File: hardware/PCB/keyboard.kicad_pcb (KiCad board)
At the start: 2 copper layers, 282.7 x 111.3 mm, 251 parts, among them U1 proton_c, U2 IS31FL3733-QF, U3 IS31FL3733-QF

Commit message: Line up most parts and fix some problems with the part
1.Fix the LED footprint size
2.Edit the hotplug to be simpler (removed 2 holes)
3.Line up everything and the silkscreen
4. Fix the LED matrix and the switch matrix sch
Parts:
- removed D139, D140, D141, D96, D97: LED_RABG, KiCad:XZMDKCBDDG45S9
- added CherryMX67: SW_SPST, KiCad:Kailh_socket_MX_simplified, F.Cu at (347.4, 167.0)
- CherryMX1, CherryMX10, CherryMX11, CherryMX12, CherryMX13, CherryMX14, CherryMX15, CherryMX16, CherryMX17, CherryMX18, CherryMX19, CherryMX2, CherryMX20, CherryMX21, CherryMX22, CherryMX23, CherryMX24, CherryMX25, CherryMX26, CherryMX27, CherryMX28, CherryMX29, CherryMX3, CherryMX30, CherryMX31, CherryMX32, CherryMX33, CherryMX34, CherryMX35, CherryMX36, CherryMX37, CherryMX38, CherryMX39, CherryMX4, CherryMX40, CherryMX41, CherryMX42, CherryMX43, CherryMX44, CherryMX45, CherryMX46, CherryMX47, CherryMX48, CherryMX49, CherryMX5, CherryMX50, CherryMX51, CherryMX52, CherryMX53, CherryMX54, CherryMX55, CherryMX56, CherryMX57, CherryMX58, CherryMX59, CherryMX6, CherryMX60, CherryMX61, CherryMX62, CherryMX63, CherryMX64, CherryMX65, CherryMX66, CherryMX68, CherryMX7, CherryMX8, CherryMX9: footprint keyswitches:Kailh_socket_MX -> KiCad:Kailh_socket_MX_simplified
- D100, D101, D102, D103, D104, D105, D106, D107, D108, D109, D110, D111, D112, D113, D114, D115, D116, D117, D118, D119, D120, D121, D122, D123, D124, D125, D126, D127, D128, D129, D130, D131, D132, D133, D134, D135, D136, D137, D138, D69, D70, D71, D72, D73, D74, D75, D76, D77, D78, D79, D80, D81, D82, D83, D84, D85, D86, D87, D88, D89, D90, D91, D92, D93, D94, D95, D98, D99: footprint KiCad:XZMDKCBDDG45S9 -> KiCad:XZMDKCBDDG45S9_fixed
- moved D67 604.6 mm to (354.3, 165.1), turned to 180 degrees
- moved D94 601.5 mm to (347.4, 162.5)
- moved D60 590.2 mm to (337.8, 106.7), turned to 180 degrees
- moved D95 589.7 mm to (347.4, 181.5)
- moved D66 585.0 mm to (356.9, 124.5), turned to 180 degrees
- moved D92 574.6 mm to (328.3, 162.5)
- moved D68 572.2 mm to (354.3, 184.2), turned to 180 degrees
- moved CherryMX66 565.8 mm to (347.4, 128.9), turned to 180 degrees
- moved D90 564.8 mm to (309.3, 162.5)
- moved D64 563.3 mm to (337.8, 182.9), turned to 180 degrees
- moved U2 557.9 mm to (353.3, 142.0), turned to 90 degrees
- moved D46 538.7 mm to (280.7, 127.0), turned to 180 degrees
- moved D86 528.4 mm to (271.2, 162.5)
- moved D44 526.6 mm to (261.6, 180.3), turned to 180 degrees
- moved D59 526.0 mm to (318.8, 182.9), turned to 180 degrees
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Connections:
- U2 pad 32: /RGB/RGBmatrix/COL15 -> Net-(U2-Pad32)
- U3 pad 32: /RGB/RGBmatrix2/COL15 -> Net-(U3-Pad32)

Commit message: I think I figured it out
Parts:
- U1: value proton_c -> Proton_C
- moved C11 339.1 mm to (404.9, 170.9)
- moved C12 335.6 mm to (404.9, 174.8)
- moved C15 331.1 mm to (394.7, 170.9)
- moved C16 328.0 mm to (394.7, 174.8)
- moved R22 327.1 mm to (389.6, 178.6)
- moved U3 324.3 mm to (399.8, 182.4)
- moved C13 323.1 mm to (399.8, 170.9)
- moved R24 322.4 mm to (384.6, 183.6)
- moved C2 321.2 mm to (384.6, 178.6)
- moved R21 319.1 mm to (384.6, 181.1)
- moved R20 318.5 mm to (389.6, 181.1)
- moved C10 310.7 mm to (387.1, 172.2)
- moved R15 305.3 mm to (389.6, 183.6)
- moved C14 289.6 mm to (399.8, 174.8)
- moved R17 266.8 mm to (388.6, 130.8)
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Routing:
- net /switch/ROW1: track 0.00 -> 291.9 mm
- net /switch/ROW4: track 0.00 -> 291.9 mm
- net /switch/ROW2: track 0.00 -> 291.9 mm
- net /switch/ROW5: track 0.00 -> 288.6 mm
- net /switch/ROW3: track 0.00 -> 278.9 mm
- net /switch/COL2: track 0.00 -> 99.3 mm, vias 0 -> 5
- net /switch/COL1: track 0.00 -> 90.9 mm, vias 0 -> 4
- net /switch/COL9: track 0.00 -> 90.9 mm, vias 0 -> 5
- net /switch/COL4: track 0.00 -> 89.2 mm, vias 0 -> 5
- net /switch/COL7: track 0.00 -> 89.2 mm, vias 0 -> 5
- net /switch/COL10: track 0.00 -> 89.2 mm, vias 0 -> 5
- net /switch/COL14: track 0.00 -> 89.2 mm, vias 0 -> 5
- net /switch/COL13: track 0.00 -> 89.2 mm, vias 0 -> 5
- net /switch/COL3: track 0.00 -> 89.2 mm, vias 0 -> 5
- net /switch/COL6: track 0.00 -> 89.2 mm, vias 0 -> 5
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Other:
- rule trace_min: 0.2 -> 0.1
- rule via_min_size: 0.4 -> 0.3

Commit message: The keys are finally connected
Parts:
- moved R15 197.3 mm to (197.6, 229.1)
- moved R20 197.3 mm to (197.6, 226.6)
- moved R22 197.3 mm to (197.6, 224.0)
- moved C10 197.3 mm to (195.1, 217.7)
- moved C13 197.3 mm to (207.8, 216.4)
- moved C14 197.3 mm to (207.8, 220.2)
- moved C15 197.3 mm to (202.7, 216.4)
- moved C16 197.3 mm to (202.7, 220.2)
- moved U3 197.3 mm to (207.8, 227.8)
- moved C11 197.3 mm to (212.9, 216.4)
- moved C12 197.3 mm to (212.9, 220.2)
- moved C2 197.3 mm to (192.5, 224.0)
- moved R21 197.3 mm to (192.5, 226.6)
- moved R24 197.3 mm to (192.5, 229.1)
- moved D1 0.25 mm to (92.5, 110.7)
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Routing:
- net /RGB/RGBmatrix2/ROW3: track 0.00 -> 288.7 mm
- net /RGB/RGBmatrix/ROW6: track 0.00 -> 288.7 mm
- net /RGB/RGBmatrix2/ROW5: track 0.00 -> 279.4 mm, vias 0 -> 24
- net /RGB/RGBmatrix/ROW9: track 0.00 -> 275.9 mm
- net /RGB/RGBmatrix2/ROW2: track 0.00 -> 274.1 mm, vias 0 -> 26
- net /RGB/RGBmatrix/ROW5: track 0.00 -> 274.1 mm, vias 0 -> 26
- net /RGB/RGBmatrix2/ROW1: track 0.00 -> 272.7 mm
- net /RGB/RGBmatrix/ROW4: track 0.00 -> 272.7 mm
- net /RGB/RGBmatrix/ROW3: track 23.2 -> 289.6 mm
- net /RGB/RGBmatrix/ROW8: track 0.00 -> 263.9 mm, vias 0 -> 23
- net /RGB/RGBmatrix/ROW7: track 0.00 -> 261.3 mm
- net /RGB/RGBmatrix/ROW2: track 21.1 -> 274.1 mm, vias 2 -> 26
- net /RGB/RGBmatrix/ROW1: track 20.9 -> 272.7 mm
- net /RGB/RGBmatrix2/ROW4: track 0.00 -> 241.8 mm
- net /RGB/RGBmatrix2/ROW6: track 0.00 -> 216.7 mm
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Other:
- net class Default: clearance 0.2 -> 0.15; trace_width 0.25 -> 0.3; via_dia 0.8 -> 1.2; via_drill 0.4 -> 0.5
- rule trace_clearance: 0.2 -> 0.15
- rule trace_min: 0.1 -> 0.3

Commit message: Make it better by get rid of the protonC
1. Remove protonC. use STM32F303CCT6 instead
2.Use parts based on avalibility
3.Extend the case so it now fits more parts( should be big enough
4. A reasonable USB connector
5. Probably a working DC-DC solution to providde 3.3V
6. Move 3733's 5V to only 3.3V (maybe it won't work?)
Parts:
- added C17: 1μF, Capacitor_SMD:C_0603_1608Metric, F.Cu at (239.6, 67.9)
- added C18: 100nF, Capacitor_SMD:C_0603_1608Metric, F.Cu at (241.2, 60.4)
- added C19: 10nF, Capacitor_SMD:C_0603_1608Metric, F.Cu at (231.6, 68.2)
- added C20: 1μF, Capacitor_SMD:C_0603_1608Metric, F.Cu at (248.7, 53.2)
- added C21: 20pF, Capacitor_SMD:C_0603_1608Metric, F.Cu at (241.2, 62.9)
- added C22: 20pF, Capacitor_SMD:C_0603_1608Metric, F.Cu at (235.6, 68.2)
- added C23: 1μF, Capacitor_SMD:C_0603_1608Metric, F.Cu at (245.2, 57.9)
- added D96: BAT60JFILM, Diode_SMD:D_SOD-323, F.Cu at (231.7, 65.4)
- added J1: USB_B_Micro, Connector_USB:USB_Micro-B_Molex-105017-0001, F.Cu at (236.9, 54.9)
- added R25: 1.5K, Resistor_SMD:R_0603_1608Metric, F.Cu at (245.2, 60.4)
- added R26: 0, Resistor_SMD:R_0603_1608Metric, F.Cu at (239.8, 65.4)
- added R27: 0, Resistor_SMD:R_0603_1608Metric, F.Cu at (235.8, 65.2)
- added R28: 100K, Resistor_SMD:R_0603_1608Metric, F.Cu at (249.2, 55.7)
- added R29: 1K, Resistor_SMD:R_0603_1608Metric, F.Cu at (249.2, 58.2)
- added R30: 10K, Resistor_SMD:R_0603_1608Metric, F.Cu at (245.2, 62.9)
- added R31: 10K, Resistor_SMD:R_0603_1608Metric, F.Cu at (249.2, 60.7)
- added R32: 0, Resistor_SMD:R_0603_1608Metric, F.Cu at (243.6, 67.9)
- added R33: 0, Resistor_SMD:R_0603_1608Metric, F.Cu at (249.2, 63.2)
- added SW1: SW_DIP_x01, Button_Switch_SMD:SW_SPST_EVQPE1, F.Cu at (225.1, 65.8)
- added U4: LD3985M33R, Package_TO_SOT_SMD:SOT-23-5, F.Cu at (244.2, 54.3)
- added Y1: YSX530GA, Crystal:Crystal_SMD_5032-2Pin_5.0x3.2mm, F.Cu at (235.6, 61.5)
- C1, C11, C13, C15, C2, C4, C6, C8: footprint Capacitor_SMD:C_0603_1608Metric_Pad1.05x0.95mm_HandSolder -> Capacitor_SMD:C_1206_3216Metric
- C10, C3: footprint Capacitor_Tantalum_SMD:CP_EIA-3528-12_Kemet-T_Pad1.50x2.35mm_HandSolder -> Capacitor_Tantalum_SMD:CP_EIA-3216-18_Kemet-A
- C12, C14, C16, C5, C7, C9: footprint Capacitor_SMD:C_0603_1608Metric_Pad1.05x0.95mm_HandSolder -> Capacitor_SMD:C_0603_1608Metric
- D1, D10, D11, D12, D13, D14, D15, D16, D17, D18, D19, D2, D20, D21, D22, D23, D24, D25, D26, D27, D28, D29, D3, D30, D31, D32, D33, D34, D35, D36, D37, D38, D39, D4, D40, D41, D42, D43, D44, D45, D46, D47, D48, D49, D5, D50, D51, D52, D53, D54, D55, D56, D57, D58, D59, D6, D60, D61, D62, D63, D64, D65, D66, D67, D68, D7, D8, D9: footprint Diode_SMD:D_SOD-123 -> Diode_SMD:D_SOD-323
- R1, R10, R11, R12, R13, R14, R15, R16, R17, R18, R19, R2, R20, R21, R22, R23, R24, R3, R4, R5, R6, R7, R8, R9: footprint Resistor_SMD:R_0603_1608Metric_Pad1.05x0.95mm_HandSolder -> Resistor_SMD:R_0603_1608Metric
- U1: value Proton_C -> STM32F303CCTx; footprint proton_c:proton_c -> Package_QFP:LQFP-48_7x7mm_P0.5mm; moved to F.Cu
- moved U3 156.4 mm to (184.8, 73.2)
- moved R15 150.6 mm to (211.5, 79.1)
- moved R20 150.6 mm to (211.5, 76.6)
- moved R21 150.6 mm to (206.4, 76.6)
- moved R24 150.6 mm to (206.4, 79.1)
- moved C2 150.6 mm to (206.4, 74.0)
- moved R22 150.6 mm to (211.5, 74.0)
- moved C12 139.8 mm to (193.5, 81.8), turned to 180 degrees
- moved C11 137.5 mm to (193.5, 80.3), turned to 180 degrees
- moved C13 136.9 mm to (186.7, 81.2)
- moved C14 136.9 mm to (186.7, 85.0)
- moved C15 136.9 mm to (181.6, 81.2)
- moved C16 136.9 mm to (181.6, 85.0)
- moved C10 135.0 mm to (199.6, 82.8)
- moved U2 108.5 mm to (294.3, 94.4)
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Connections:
- C1 pad 2: VCC -> +3V3
- C10 pad 1: VBUS -> +3V3
- C11 pad 1: VBUS -> +3V3
- C12 pad 1: VBUS -> +3V3
- C13 pad 1: VBUS -> +3V3
- C14 pad 1: VBUS -> +3V3
- C15 pad 1: VBUS -> +3V3
- C16 pad 1: VBUS -> +3V3
- C2 pad 2: VCC -> +3V3
- C3 pad 1: VBUS -> +3V3
- C4 pad 1: VBUS -> +3V3
- C5 pad 1: VBUS -> +3V3
- C6 pad 1: VBUS -> +3V3
- C7 pad 1: VBUS -> +3V3
- C8 pad 1: VBUS -> +3V3
- C9 pad 1: VBUS -> +3V3
- CherryMX1 pad 1: /switch/ROW1 -> /SMT32/ROW1
- CherryMX10 pad 1: /switch/ROW5 -> /SMT32/ROW5
- CherryMX11 pad 1: /switch/ROW1 -> /SMT32/ROW1
- CherryMX12 pad 1: /switch/ROW2 -> /SMT32/ROW2
- CherryMX13 pad 1: /switch/ROW3 -> /SMT32/ROW3
- CherryMX14 pad 1: /switch/ROW4 -> /SMT32/ROW4
- CherryMX15 pad 1: /switch/ROW5 -> /SMT32/ROW5
- CherryMX16 pad 1: /switch/ROW1 -> /SMT32/ROW1
- CherryMX17 pad 1: /switch/ROW2 -> /SMT32/ROW2
- CherryMX18 pad 1: /switch/ROW3 -> /SMT32/ROW3
- CherryMX19 pad 1: /switch/ROW4 -> /SMT32/ROW4
- CherryMX2 pad 1: /switch/ROW2 -> /SMT32/ROW2
- CherryMX20 pad 1: /switch/ROW5 -> /SMT32/ROW5
- CherryMX21 pad 1: /switch/ROW1 -> /SMT32/ROW1
- CherryMX22 pad 1: /switch/ROW2 -> /SMT32/ROW2
- CherryMX23 pad 1: /switch/ROW3 -> /SMT32/ROW3
- CherryMX24 pad 1: /switch/ROW4 -> /SMT32/ROW4
- CherryMX25 pad 1: /switch/ROW5 -> /SMT32/ROW5
- CherryMX26 pad 1: /switch/ROW1 -> /SMT32/ROW1
- CherryMX27 pad 1: /switch/ROW2 -> /SMT32/ROW2
- CherryMX28 pad 1: /switch/ROW3 -> /SMT32/ROW3
- CherryMX29 pad 1: /switch/ROW4 -> /SMT32/ROW4
- CherryMX3 pad 1: /switch/ROW3 -> /SMT32/ROW3
- CherryMX30 pad 1: /switch/ROW5 -> /SMT32/ROW5
- CherryMX31 pad 1: /switch/ROW1 -> /SMT32/ROW1
- CherryMX32 pad 1: /switch/ROW2 -> /SMT32/ROW2
- CherryMX33 pad 1: /switch/ROW3 -> /SMT32/ROW3
- CherryMX34 pad 1: /switch/ROW4 -> /SMT32/ROW4
- CherryMX35 pad 1: /switch/ROW1 -> /SMT32/ROW1
- CherryMX36 pad 1: /switch/ROW2 -> /SMT32/ROW2
- CherryMX37 pad 1: /switch/ROW3 -> /SMT32/ROW3
- CherryMX38 pad 1: /switch/ROW4 -> /SMT32/ROW4
- CherryMX39 pad 1: /switch/ROW5 -> /SMT32/ROW5
- CherryMX4 pad 1: /switch/ROW4 -> /SMT32/ROW4
- CherryMX40 pad 1: /switch/ROW1 -> /SMT32/ROW1
- CherryMX41 pad 1: /switch/ROW2 -> /SMT32/ROW2
- CherryMX42 pad 1: /switch/ROW3 -> /SMT32/ROW3
- CherryMX43 pad 1: /switch/ROW4 -> /SMT32/ROW4
- CherryMX44 pad 1: /switch/ROW5 -> /SMT32/ROW5
- CherryMX45 pad 1: /switch/ROW1 -> /SMT32/ROW1
- CherryMX46 pad 1: /switch/ROW2 -> /SMT32/ROW2
- CherryMX47 pad 1: /switch/ROW3 -> /SMT32/ROW3
- CherryMX48 pad 1: /switch/ROW4 -> /SMT32/ROW4
- CherryMX49 pad 1: /switch/ROW5 -> /SMT32/ROW5
- CherryMX5 pad 1: /switch/ROW5 -> /SMT32/ROW5
- CherryMX50 pad 1: /switch/ROW1 -> /SMT32/ROW1
- CherryMX51 pad 1: /switch/ROW2 -> /SMT32/ROW2
- CherryMX52 pad 1: /switch/ROW3 -> /SMT32/ROW3
- CherryMX53 pad 1: /switch/ROW4 -> /SMT32/ROW4
- CherryMX54 pad 1: /switch/ROW5 -> /SMT32/ROW5
- CherryMX55 pad 1: /switch/ROW1 -> /SMT32/ROW1
- CherryMX56 pad 1: /switch/ROW2 -> /SMT32/ROW2
- CherryMX57 pad 1: /switch/ROW3 -> /SMT32/ROW3
- CherryMX58 pad 1: /switch/ROW4 -> /SMT32/ROW4
- CherryMX59 pad 1: /switch/ROW5 -> /SMT32/ROW5
- CherryMX6 pad 1: /switch/ROW1 -> /SMT32/ROW1
- CherryMX60 pad 1: /switch/ROW1 -> /SMT32/ROW1
- CherryMX61 pad 1: /switch/ROW2 -> /SMT32/ROW2
- CherryMX62 pad 1: /switch/ROW3 -> /SMT32/ROW3
- CherryMX63 pad 1: /switch/ROW4 -> /SMT32/ROW4
- CherryMX64 pad 1: /switch/ROW5 -> /SMT32/ROW5
- CherryMX65 pad 1: /switch/ROW1 -> /SMT32/ROW1
- CherryMX66 pad 1: /switch/ROW2 -> /SMT32/ROW2
- CherryMX67 pad 1: /switch/ROW4 -> /SMT32/ROW4
- CherryMX68 pad 1: /switch/ROW5 -> /SMT32/ROW5
- CherryMX7 pad 1: /switch/ROW2 -> /SMT32/ROW2
- CherryMX8 pad 1: /switch/ROW3 -> /SMT32/ROW3
- CherryMX9 pad 1: /switch/ROW4 -> /SMT32/ROW4
- D1 pad 1: /switch/COL14 -> /SMT32/COL14
- D10 pad 1: /switch/COL13 -> /SMT32/COL13
- D11 pad 1: /switch/COL12 -> /SMT32/COL12
- D12 pad 1: /switch/COL12 -> /SMT32/COL12
- D13 pad 1: /switch/COL12 -> /SMT32/COL12
- D14 pad 1: /switch/COL12 -> /SMT32/COL12
- D15 pad 1: /switch/COL12 -> /SMT32/COL12
- D16 pad 1: /switch/COL11 -> /SMT32/COL11
- D17 pad 1: /switch/COL11 -> /SMT32/COL11
- D18 pad 1: /switch/COL11 -> /SMT32/COL11
- D19 pad 1: /switch/COL11 -> /SMT32/COL11
- D2 pad 1: /switch/COL14 -> /SMT32/COL14
- D20 pad 1: /switch/COL11 -> /SMT32/COL11
- D21 pad 1: /switch/COL10 -> /SMT32/COL10
- D22 pad 1: /switch/COL10 -> /SMT32/COL10
- D23 pad 1: /switch/COL10 -> /SMT32/COL10
- D24 pad 1: /switch/COL10 -> /SMT32/COL10
- D25 pad 1: /switch/COL10 -> /SMT32/COL10
- D26 pad 1: /switch/COL9 -> /SMT32/COL9
- D27 pad 1: /switch/COL9 -> /SMT32/COL9
- D28 pad 1: /switch/COL9 -> /SMT32/COL9
- D29 pad 1: /switch/COL9 -> /SMT32/COL9
- D3 pad 1: /switch/COL14 -> /SMT32/COL14
- D30 pad 1: /switch/COL9 -> /SMT32/COL9
- D31 pad 1: /switch/COL8 -> /SMT32/COL8
- D32 pad 1: /switch/COL8 -> /SMT32/COL8
- D33 pad 1: /switch/COL8 -> /SMT32/COL8
- D34 pad 1: /switch/COL8 -> /SMT32/COL8
- D35 pad 1: /switch/COL7 -> /SMT32/COL7
- D36 pad 1: /switch/COL7 -> /SMT32/COL7
- D37 pad 1: /switch/COL7 -> /SMT32/COL7
- D38 pad 1: /switch/COL7 -> /SMT32/COL7
- D39 pad 1: /switch/COL7 -> /SMT32/COL7
- D4 pad 1: /switch/COL14 -> /SMT32/COL14
- D40 pad 1: /switch/COL6 -> /SMT32/COL6
- D41 pad 1: /switch/COL6 -> /SMT32/COL6
- D42 pad 1: /switch/COL6 -> /SMT32/COL6
- D43 pad 1: /switch/COL6 -> /SMT32/COL6
- D44 pad 1: /switch/COL6 -> /SMT32/COL6
- D45 pad 1: /switch/COL5 -> /SMT32/COL5
- D46 pad 1: /switch/COL5 -> /SMT32/COL5
- D47 pad 1: /switch/COL5 -> /SMT32/COL5
- D48 pad 1: /switch/COL5 -> /SMT32/COL5
- D49 pad 1: /switch/COL5 -> /SMT32/COL5
- D5 pad 1: /switch/COL14 -> /SMT32/COL14
- D50 pad 1: /switch/COL4 -> /SMT32/COL4
- D51 pad 1: /switch/COL4 -> /SMT32/COL4
- D52 pad 1: /switch/COL4 -> /SMT32/COL4
- D53 pad 1: /switch/COL4 -> /SMT32/COL4
- D54 pad 1: /switch/COL4 -> /SMT32/COL4
- D55 pad 1: /switch/COL3 -> /SMT32/COL3
- D56 pad 1: /switch/COL3 -> /SMT32/COL3
- D57 pad 1: /switch/COL3 -> /SMT32/COL3
- D58 pad 1: /switch/COL3 -> /SMT32/COL3
- D59 pad 1: /switch/COL3 -> /SMT32/COL3
- D6 pad 1: /switch/COL13 -> /SMT32/COL13
- D60 pad 1: /switch/COL2 -> /SMT32/COL2
- D61 pad 1: /switch/COL2 -> /SMT32/COL2
- D62 pad 1: /switch/COL2 -> /SMT32/COL2
- D63 pad 1: /switch/COL2 -> /SMT32/COL2
- D64 pad 1: /switch/COL2 -> /SMT32/COL2
- D65 pad 1: /switch/COL1 -> /SMT32/COL1
- D66 pad 1: /switch/COL1 -> /SMT32/COL1
- D67 pad 1: /switch/COL1 -> /SMT32/COL1
- D68 pad 1: /switch/COL1 -> /SMT32/COL1
- D7 pad 1: /switch/COL13 -> /SMT32/COL13
- D8 pad 1: /switch/COL13 -> /SMT32/COL13
- D9 pad 1: /switch/COL13 -> /SMT32/COL13
- R1 pad 1: /switch/COL1 -> /SMT32/COL1
- R1 pad 2: VCC -> +3V3
- R10 pad 1: /switch/COL10 -> /SMT32/COL10
- R10 pad 2: VCC -> +3V3
- R11 pad 1: /switch/COL11 -> /SMT32/COL11
- R11 pad 2: VCC -> +3V3
- R12 pad 1: /switch/COL12 -> /SMT32/COL12
- R12 pad 2: VCC -> +3V3
- R13 pad 1: /switch/COL13 -> /SMT32/COL13
- R13 pad 2: VCC -> +3V3
- R14 pad 1: /switch/COL14 -> /SMT32/COL14
- R14 pad 2: VCC -> +3V3
- R17 pad 1: VCC -> +3V3
- R17 pad 2: /RGB/SDA -> /SMT32/I2C2_SDA
- R18 pad 1: VCC -> +3V3
- R18 pad 2: /RGB/SCL -> /SMT32/I2C2_SCL
- R2 pad 1: /switch/COL2 -> /SMT32/COL2
- R2 pad 2: VCC -> +3V3
- R20 pad 1: VCC -> +3V3
- R20 pad 2: /RGB/SCL -> /SMT32/I2C2_SCL
- R21 pad 1: VCC -> +3V3
- R21 pad 2: /RGB/SDA -> /SMT32/I2C2_SDA
- R3 pad 1: /switch/COL3 -> /SMT32/COL3
- R3 pad 2: VCC -> +3V3
- R4 pad 1: /switch/COL4 -> /SMT32/COL4
- R4 pad 2: VCC -> +3V3
- R5 pad 1: /switch/COL5 -> /SMT32/COL5
- R5 pad 2: VCC -> +3V3
- R6 pad 1: /switch/COL6 -> /SMT32/COL6
- R6 pad 2: VCC -> +3V3
- R7 pad 1: /switch/COL7 -> /SMT32/COL7
- R7 pad 2: VCC -> +3V3
- R8 pad 1: /switch/COL8 -> /SMT32/COL8
- R8 pad 2: VCC -> +3V3
- R9 pad 1: /switch/COL9 -> /SMT32/COL9
- R9 pad 2: VCC -> +3V3
- U2 pad 20: VBUS -> +3V3
- U2 pad 29: VBUS -> +3V3
- U2 pad 37: VBUS -> +3V3
- U2 pad 38: VBUS -> +3V3
- U2 pad 39: VCC -> +3V3
- U2 pad 41: /RGB/SDA -> /SMT32/I2C2_SDA
- U2 pad 42: /RGB/SCL -> /SMT32/I2C2_SCL
- U3 pad 20: VBUS -> +3V3
- U3 pad 29: VBUS -> +3V3
- U3 pad 37: VBUS -> +3V3
- U3 pad 38: VBUS -> +3V3
- U3 pad 39: VCC -> +3V3
- U3 pad 41: /RGB/SDA -> /SMT32/I2C2_SDA
- U3 pad 42: /RGB/SCL -> /SMT32/I2C2_SCL
- U3 pad 43: VBUS -> +3V3
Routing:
- net /SMT32/ROW5: track 0.00 -> 306.0 mm
- net /switch/ROW1: track 291.9 -> 0.00 mm
- net /SMT32/ROW1: track 0.00 -> 291.9 mm
- net /switch/ROW4: track 291.9 -> 0.00 mm
- net /SMT32/ROW4: track 0.00 -> 291.9 mm
- net /switch/ROW2: track 291.9 -> 0.00 mm
- net /SMT32/ROW2: track 0.00 -> 291.9 mm
- net /switch/ROW5: track 288.6 -> 0.00 mm
- net /switch/ROW3: track 278.9 -> 0.00 mm
- net /SMT32/ROW3: track 0.00 -> 278.9 mm
- net /switch/COL2: track 99.2 -> 0.00 mm, vias 5 -> 0
- net /switch/COL9: track 97.3 -> 0.13 mm, vias 5 -> 0
- net /switch/COL1: track 94.2 -> 0.00 mm, vias 4 -> 0
- net /switch/COL4: track 89.0 -> 0.00 mm, vias 5 -> 0
- net /switch/COL7: track 89.0 -> 0.00 mm, vias 5 -> 0
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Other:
- board size 282.7 x 111.3 mm -> 282.7 x 117.3 mm
- rule trace_min: 0.3 -> 0.127

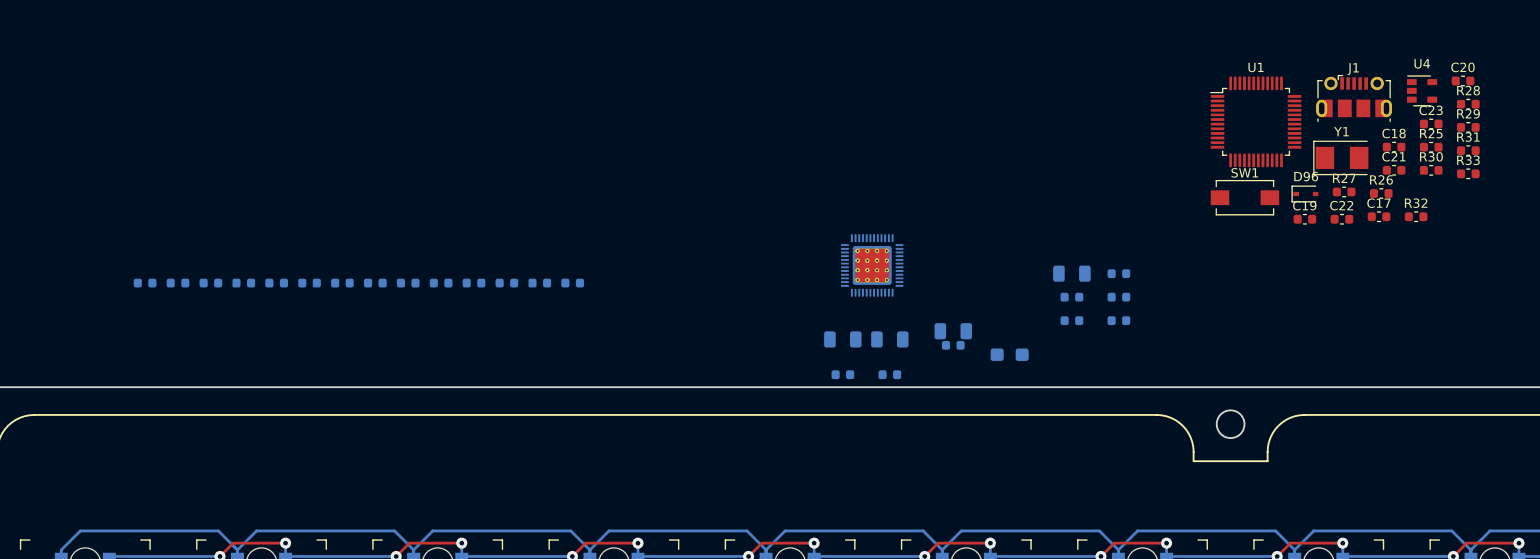
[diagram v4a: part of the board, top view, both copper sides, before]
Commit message: I think I don't need those pull ups, if i really need it, add them later
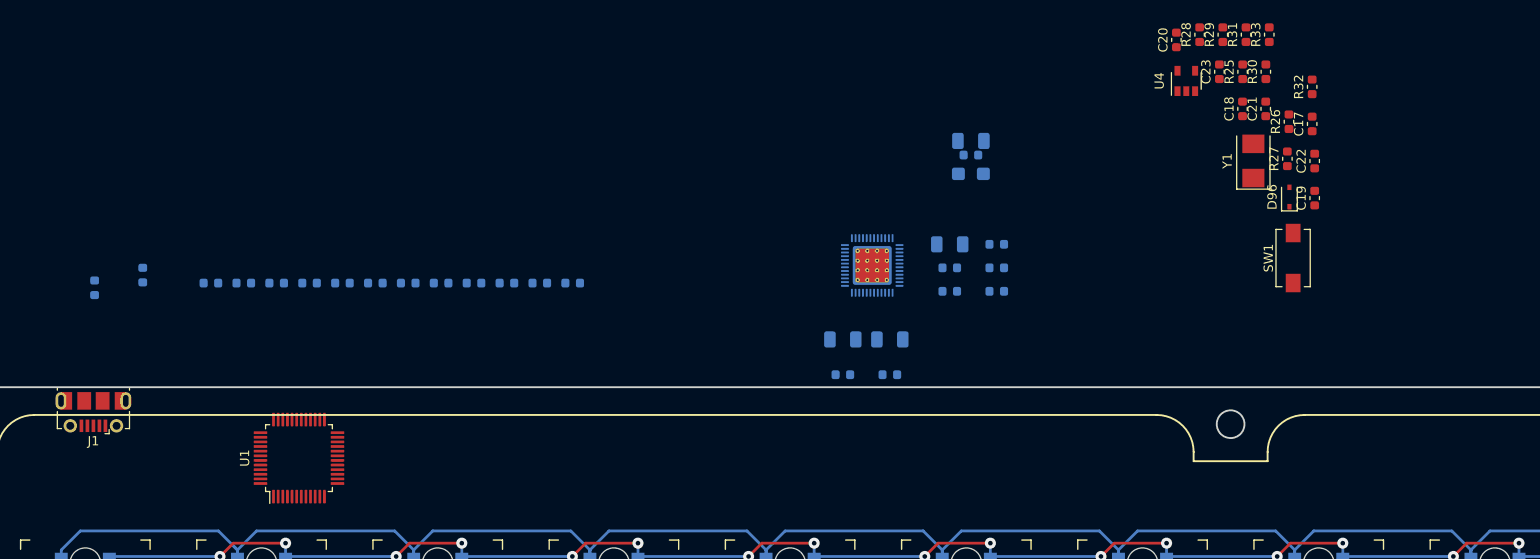
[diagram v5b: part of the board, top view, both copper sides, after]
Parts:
- moved J1 140.5 mm to (100.6, 89.0), turned to 180 degrees
- moved U1 109.7 mm to (122.8, 94.0), turned to 90 degrees
- moved C20 31.3 mm to (217.7, 48.8), turned to 90 degrees
- moved R28 30.0 mm to (220.2, 48.2), turned to 90 degrees
- moved R29 28.4 mm to (222.7, 48.2), turned to 90 degrees
- moved R31 27.1 mm to (225.2, 48.2), turned to 90 degrees
- moved R33 26.3 mm to (227.7, 48.2), turned to 90 degrees
- moved U4 25.5 mm to (218.7, 53.2), turned to 90 degrees
- moved C23 23.6 mm to (222.3, 52.2), turned to 90 degrees
- moved R25 22.0 mm to (224.8, 52.2), turned to 90 degrees
- moved R30 20.8 mm to (227.3, 52.2), turned to 90 degrees
- moved C11 20.7 mm to (195.5, 59.7)
- moved C12 20.7 mm to (195.5, 61.2)
- moved C10 20.0 mm to (195.5, 63.2), turned to 180 degrees
- moved R32 18.0 mm to (232.4, 53.8), turned to 90 degrees
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
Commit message: clear all the traces
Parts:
- removed R1, R10, R11, R12, R13, R14, R2, R3, R4, R5, R6, R7, R8, R9: 10k, Resistor_SMD:R_0603_1608Metric
- added C24: 100nF, Capacitor_SMD:C_0603_1608Metric, B.Cu at (177.4, 64.0)
- added C25: 100nF, Capacitor_SMD:C_0603_1608Metric, B.Cu at (177.4, 61.5)
- added C26: 100nF, Capacitor_SMD:C_0603_1608Metric, B.Cu at (181.4, 64.0)
- added C27: 100nF, Capacitor_SMD:C_0603_1608Metric, B.Cu at (181.4, 61.5)
- C17, C18, C19, C20, C21, C22, C23, D96, J1, R25, R26, R27, R28, R29, R30, R31, R32, R33, SW1, U1, U4, Y1: moved to B.Cu
- moved SW1 95.7 mm to (134.8, 66.9), turned to 0 degrees
- moved C19 91.4 mm to (141.3, 64.6), turned to 0 degrees
- moved D96 88.5 mm to (141.4, 67.3), turned to 0 degrees
- moved C22 87.4 mm to (145.3, 64.6), turned to 0 degrees
- moved R27 84.4 mm to (145.5, 67.5), turned to 0 degrees
- moved C17 83.4 mm to (149.3, 64.8), turned to 0 degrees
- moved Y1 81.2 mm to (145.3, 71.2), turned to 0 degrees
- moved R26 80.9 mm to (149.5, 67.3), turned to 0 degrees
- moved R32 79.8 mm to (153.3, 64.8), turned to 0 degrees
- moved C18 78.9 mm to (149.7, 80.4), turned to 0 degrees
- moved R31 78.6 mm to (153.3, 80.0), turned to 0 degrees
- moved C21 77.6 mm to (150.9, 69.8), turned to 0 degrees
- moved R25 76.0 mm to (153.3, 77.9), turned to 0 degrees
- moved R30 74.5 mm to (154.9, 69.8), turned to 0 degrees
- moved R29 73.3 mm to (156.8, 80.4), turned to 0 degrees
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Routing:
- net /SMT32/ROW5: track 306.0 -> 0.00 mm
- net /SMT32/ROW1: track 291.9 -> 0.00 mm
- net /SMT32/ROW4: track 291.9 -> 0.00 mm
- net /SMT32/ROW2: track 291.9 -> 0.00 mm
- net /RGB/RGBmatrix/ROW3: track 289.6 -> 0.00 mm
- net /RGB/RGBmatrix2/ROW3: track 288.7 -> 0.00 mm
- net /RGB/RGBmatrix/ROW6: track 288.7 -> 0.00 mm
- net /RGB/RGBmatrix2/ROW6: track 279.3 -> 0.00 mm
- net /SMT32/ROW3: track 278.9 -> 0.00 mm
- net /RGB/RGBmatrix/ROW9: track 275.9 -> 0.00 mm
- net /RGB/RGBmatrix2/ROW4: track 274.7 -> 0.00 mm, vias 1 -> 0
- net /RGB/RGBmatrix2/ROW2: track 274.1 -> 0.00 mm, vias 26 -> 0
- net /RGB/RGBmatrix/ROW5: track 274.1 -> 0.00 mm, vias 26 -> 0
- net /RGB/RGBmatrix/ROW2: track 274.1 -> 0.00 mm, vias 26 -> 0
- net /RGB/RGBmatrix/ROW1: track 272.7 -> 0.00 mm
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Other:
- net class Default: via_dia 1.2 -> 0.8; via_drill 0.5 -> 0.35
- net class Power added: clearance 0.15, trace_width 0.3, via_dia 0.8, via_drill 0.35
- net class RGB_Power added: clearance 0.15, trace_width 0.2, via_dia 0.8, via_drill 0.35
- net class Signal added: clearance 0.15, trace_width 0.2, via_dia 0.6, via_drill 0.35

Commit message: PSU placed
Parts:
- added TP1: TestPoint, TestPoint:TestPoint_Pad_D1.0mm, B.Cu at (110.0, 76.8)
- added TP2: TestPoint, TestPoint:TestPoint_Pad_D1.0mm, B.Cu at (105.2, 81.4)
- added TP3: TestPoint, TestPoint:TestPoint_Pad_D1.0mm, B.Cu at (96.3, 93.6)
- added TP4: TestPoint, TestPoint:TestPoint_Pad_D1.0mm, B.Cu at (118.6, 72.8)
- added TP5: TestPoint, TestPoint:TestPoint_Pad_D1.0mm, B.Cu at (121.7, 75.8)
- C1, C11, C13, C15, C2, C4, C6, C8: footprint Capacitor_SMD:C_1206_3216Metric -> Capacitor_SMD:C_0402_1005Metric
- C12, C14, C16, C17, C20, C21, C22, C23, C5, C7, C9: footprint Capacitor_SMD:C_0603_1608Metric -> Capacitor_SMD:C_0402_1005Metric
- C18, C24, C25, C26, C27: value 100nF -> 0.1μF; footprint Capacitor_SMD:C_0603_1608Metric -> Capacitor_SMD:C_0402_1005Metric
- C19: value 10nF -> 0.01μF; footprint Capacitor_SMD:C_0603_1608Metric -> Capacitor_SMD:C_0402_1005Metric
- R15, R16, R17, R18, R19, R20, R21, R22, R23, R24, R25, R28, R29, R30, R31, R32, R33: footprint Resistor_SMD:R_0603_1608Metric -> Resistor_SMD:R_0402_1005Metric
- R26, R27: value 0 -> 22; footprint Resistor_SMD:R_0603_1608Metric -> Resistor_SMD:R_0402_1005Metric; moved to F.Cu
- U1: moved to F.Cu
- moved J1 236.2 mm to (334.9, 89.0)
- moved C19 204.2 mm to (343.8, 91.1)
- moved D96 203.9 mm to (343.3, 95.9), turned to 270 degrees
- moved C17 188.8 mm to (335.9, 93.1), turned to 180 degrees
- moved C18 186.7 mm to (335.9, 94.1), turned to 180 degrees
- moved R27 182.5 mm to (326.0, 94.6), turned to 180 degrees
- moved U1 178.9 mm to (317.8, 95.1)
- moved U4 178.6 mm to (340.8, 92.1)
- moved R26 178.4 mm to (326.0, 93.6)
- moved C20 177.1 mm to (343.8, 93.1)
- moved U2 64.1 mm to (280.7, 79.4)
- moved C5 52.8 mm to (292.9, 62.5)
- moved C7 52.8 mm to (288.3, 62.5)
- moved C9 52.8 mm to (283.7, 62.5)
- moved C4 52.8 mm to (293.5, 58.9)
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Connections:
- J1 pad 2: Net-(J1-Pad2) -> /SMT32/USB_D-
- J1 pad 3: Net-(J1-Pad3) -> /SMT32/USB_D+
- R25 pad 1: Net-(J1-Pad2) -> /SMT32/USB_D-
- R26 pad 1: /SMT32/USB_DP -> Net-(R26-Pad1)
- R26 pad 2: Net-(J1-Pad3) -> /SMT32/USB_D-
- R27 pad 1: Net-(J1-Pad2) -> /SMT32/USB_D+
- R27 pad 2: /SMT32/USB_DM -> Net-(R27-Pad2)
- U1 pad 32: /SMT32/USB_DP -> Net-(R27-Pad2)
- U1 pad 33: /SMT32/USB_DM -> Net-(R26-Pad1)
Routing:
- net GND: track 0.00 -> 30.2 mm
- net +5V: track 0.00 -> 16.6 mm, vias 0 -> 2
- net /SMT32/USB_D+: track 0.00 -> 15.6 mm, vias 0 -> 1
- net /SMT32/USB_D-: track 0.00 -> 14.2 mm, vias 0 -> 1
- net Net-(R26-Pad1): track 0.00 -> 3.72 mm
- net Net-(R27-Pad2): track 0.00 -> 3.71 mm
- net Net-(C20-Pad1): track 0.00 -> 3.12 mm
- net Net-(CherryMX30-Pad2): track 0.00 -> 1.99 mm
- net Net-(CherryMX3-Pad2): track 0.00 -> 1.98 mm
- net Net-(CherryMX4-Pad2): track 0.00 -> 1.98 mm
- net Net-(CherryMX2-Pad2): track 0.00 -> 1.98 mm
- net Net-(CherryMX1-Pad2): track 0.00 -> 1.98 mm
- net Net-(CherryMX62-Pad2): track 0.00 -> 1.98 mm
- net Net-(CherryMX5-Pad2): track 0.00 -> 1.98 mm
- net Net-(CherryMX37-Pad2): track 0.00 -> 1.98 mm
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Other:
- rule via_min_size: 0.3 -> 0.6
